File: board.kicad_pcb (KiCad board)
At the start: 4 copper layers, 100 x 100 mm, 90 parts, among them J1 IN1, J2 IN2, J3 OUT1, J4 OUT2, U1 MFRC52202HN1,151, U2 SN74HC595N, U3 MFRC52202HN1,151, U4 MFRC52202HN1,151, U5 MFRC52202HN1,151, Y1 27.12 MHz Crystal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

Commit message: Previous stuff and im now at a point where a single reader circuit should be ready for replecation
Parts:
- removed C14, C16, C30, C44: 100nF, Capacitor_SMD:C_0603_1608Metric
- added C58: 100nF, Capacitor_SMD:C_0603_1608Metric, F.Cu at (104.4, 85.2)
- added C59: 100nF, Capacitor_SMD:C_0603_1608Metric, F.Cu at (214.0, 132.2)
- added C60: 100nF, Capacitor_SMD:C_0603_1608Metric, F.Cu at (184.1, 53.0)
- added C61: 100nF, Capacitor_SMD:C_0603_1608Metric, F.Cu at (190.8, 106.5)
- added C62: 100nF, Capacitor_SMD:C_0603_1608Metric, F.Cu at (100.0, 85.4)
- added C63: 100nF, Capacitor_SMD:C_0603_1608Metric, F.Cu at (214.0, 129.0)
- added C64: 100nF, Capacitor_SMD:C_0603_1608Metric, F.Cu at (187.3, 53.0)
- added C65: 100nF, Capacitor_SMD:C_0603_1608Metric, F.Cu at (190.8, 109.8)
- added C66: 1uF, Capacitor_SMD:C_0603_1608Metric, F.Cu at (104.2, 76.8)
- added C67: 1uF, Capacitor_SMD:C_0603_1608Metric, F.Cu at (223.0, 133.0)
- added C68: 1uF, Capacitor_SMD:C_0603_1608Metric, F.Cu at (183.3, 62.0)
- added C69: 1uF, Capacitor_SMD:C_0603_1608Metric, F.Cu at (181.8, 105.8)
- added R13: 10k, Resistor_SMD:R_0603_1608Metric, F.Cu at (97.7, 87.0)
- added R14: 10k, Resistor_SMD:R_0603_1608Metric, F.Cu at (213.2, 125.0)
- added R15: 10k, Resistor_SMD:R_0603_1608Metric, F.Cu at (191.3, 52.3)
- added R16: 10k, Resistor_SMD:R_0603_1608Metric, F.Cu at (191.5, 113.8)
- J1: footprint Connector_PinSocket_2.54mm:PinSocket_1x09_P2.54mm_Horizontal -> Connector_PinSocket_2.54mm:PinSocket_1x10_P2.54mm_Horizontal
- J2: value IN2 -> OUT1; footprint Connector_PinSocket_2.54mm:PinSocket_1x09_P2.54mm_Horizontal -> Connector_PinSocket_2.54mm:PinSocket_1x10_P2.54mm_Horizontal
- J3: value OUT1 -> IN2; footprint Connector_PinHeader_2.54mm:PinHeader_1x09_P2.54mm_Horizontal -> Connector_PinSocket_2.54mm:PinSocket_1x10_P2.54mm_Horizontal
- J4: footprint Connector_PinHeader_2.54mm:PinHeader_1x09_P2.54mm_Horizontal -> Connector_PinSocket_2.54mm:PinSocket_1x10_P2.54mm_Horizontal
- moved U3 105.5 mm to (218.0, 130.0)
- moved U5 104.2 mm to (186.8, 108.8)
- moved U4 104.2 mm to (186.3, 57.0)
- moved C52 84.3 mm to (183.0, 116.0), turned to 180 degrees
- moved C46 81.6 mm to (190.0, 113.8), turned to -90 degrees
- moved C47 81.0 mm to (186.5, 116.5)
- moved L7 80.5 mm to (182.0, 107.5), turned to 180 degrees
- moved C50 80.4 mm to (177.0, 107.5), turned to 180 degrees
- moved C45 80.3 mm to (180.8, 111.8), turned to -90 degrees
- moved C43 79.8 mm to (188.5, 104.8), turned to 180 degrees
- moved L8 79.7 mm to (182.0, 109.2), turned to 180 degrees
- moved C51 79.7 mm to (177.0, 109.2), turned to 180 degrees
- moved Y4 78.6 mm to (187.0, 113.8)
- moved R11 77.2 mm to (182.2, 111.8), turned to -90 degrees
- moved R12 76.6 mm to (183.8, 113.5), turned to -90 degrees
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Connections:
- C11 pad 1: Net-(C11-Pad1) -> Net-(C10-Pad1)
- C12 pad 2: Net-(C11-Pad1) -> Net-(C10-Pad1)
- C23 pad 2: Net-(C23-Pad2) -> Net-(C22-Pad2)
- C26 pad 1: Net-(C23-Pad2) -> Net-(C22-Pad2)
- C28 pad 2: Net-(C23-Pad2) -> Net-(C22-Pad2)
- C37 pad 2: Net-(C37-Pad2) -> Net-(C36-Pad2)
- C40 pad 1: Net-(C37-Pad2) -> Net-(C36-Pad2)
- C42 pad 2: Net-(C37-Pad2) -> Net-(C36-Pad2)
- C51 pad 2: Net-(C51-Pad2) -> Net-(C50-Pad2)
- C54 pad 1: Net-(C51-Pad2) -> Net-(C50-Pad2)
- C56 pad 2: Net-(C51-Pad2) -> Net-(C50-Pad2)
- C8 pad 2: Net-(C11-Pad1) -> Net-(C10-Pad1)
- J1 pad 7: /Sub Board/SRCLK -> /Sub Board/OE
- J1 pad 8: /Sub Board/RCLK -> /Sub Board/SRCLK
- J1 pad 9: /Sub Board/SER -> /Sub Board/RCLK
- J2 pad 7: /Sub Board/SRCLK -> /Sub Board/OE
- J2 pad 8: /Sub Board/RCLK -> /Sub Board/SRCLK
- J2 pad 9: /Sub Board/SER -> /Sub Board/RCLK
- J3 pad 7: /Sub Board/SRCLK -> /Sub Board/OE
- J3 pad 8: /Sub Board/RCLK -> /Sub Board/SRCLK
- J3 pad 9: /Sub Board/SER_OUT -> /Sub Board/RCLK
- J4 pad 7: /Sub Board/SRCLK -> /Sub Board/OE
- J4 pad 8: /Sub Board/RCLK -> /Sub Board/SRCLK
- J4 pad 9: /Sub Board/SER_OUT -> /Sub Board/RCLK
- U2 pad 13: GND -> /Sub Board/OE
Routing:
- net Net-(C10-Pad1): track 17.1 -> 482.1 mm, vias 2 -> 4
- net GND: track 42.0 -> 153.2 mm, vias 26 -> 101
- net +3V3: track 8.26 -> 47.4 mm, vias 5 -> 22
- net Net-(C50-Pad2): track 0.00 -> 20.5 mm, vias 0 -> 2
- net Net-(C22-Pad2): track 0.00 -> 20.5 mm, vias 0 -> 2
- net Net-(C36-Pad2): track 0.00 -> 20.5 mm, vias 0 -> 2
- net Net-(U3-OSCIN): track 0.00 -> 5.78 mm
- net Net-(U5-OSCIN): track 0.00 -> 5.78 mm
- net Net-(U4-OSCIN): track 0.00 -> 5.78 mm
- net /Sub Board/RC522-1/MFSDA-CS: track 0.00 -> 4.95 mm, vias 0 -> 2
- net /Sub Board/RST: track 1.68 -> 6.37 mm
- net Net-(U4-OSCOUT): track 0.00 -> 3.83 mm
- net Net-(U3-OSCOUT): track 0.00 -> 3.83 mm
- net Net-(U5-OSCOUT): track 0.00 -> 3.83 mm
- net /Sub Board/RC522-3/VMID: track 0.00 -> 3.70 mm
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
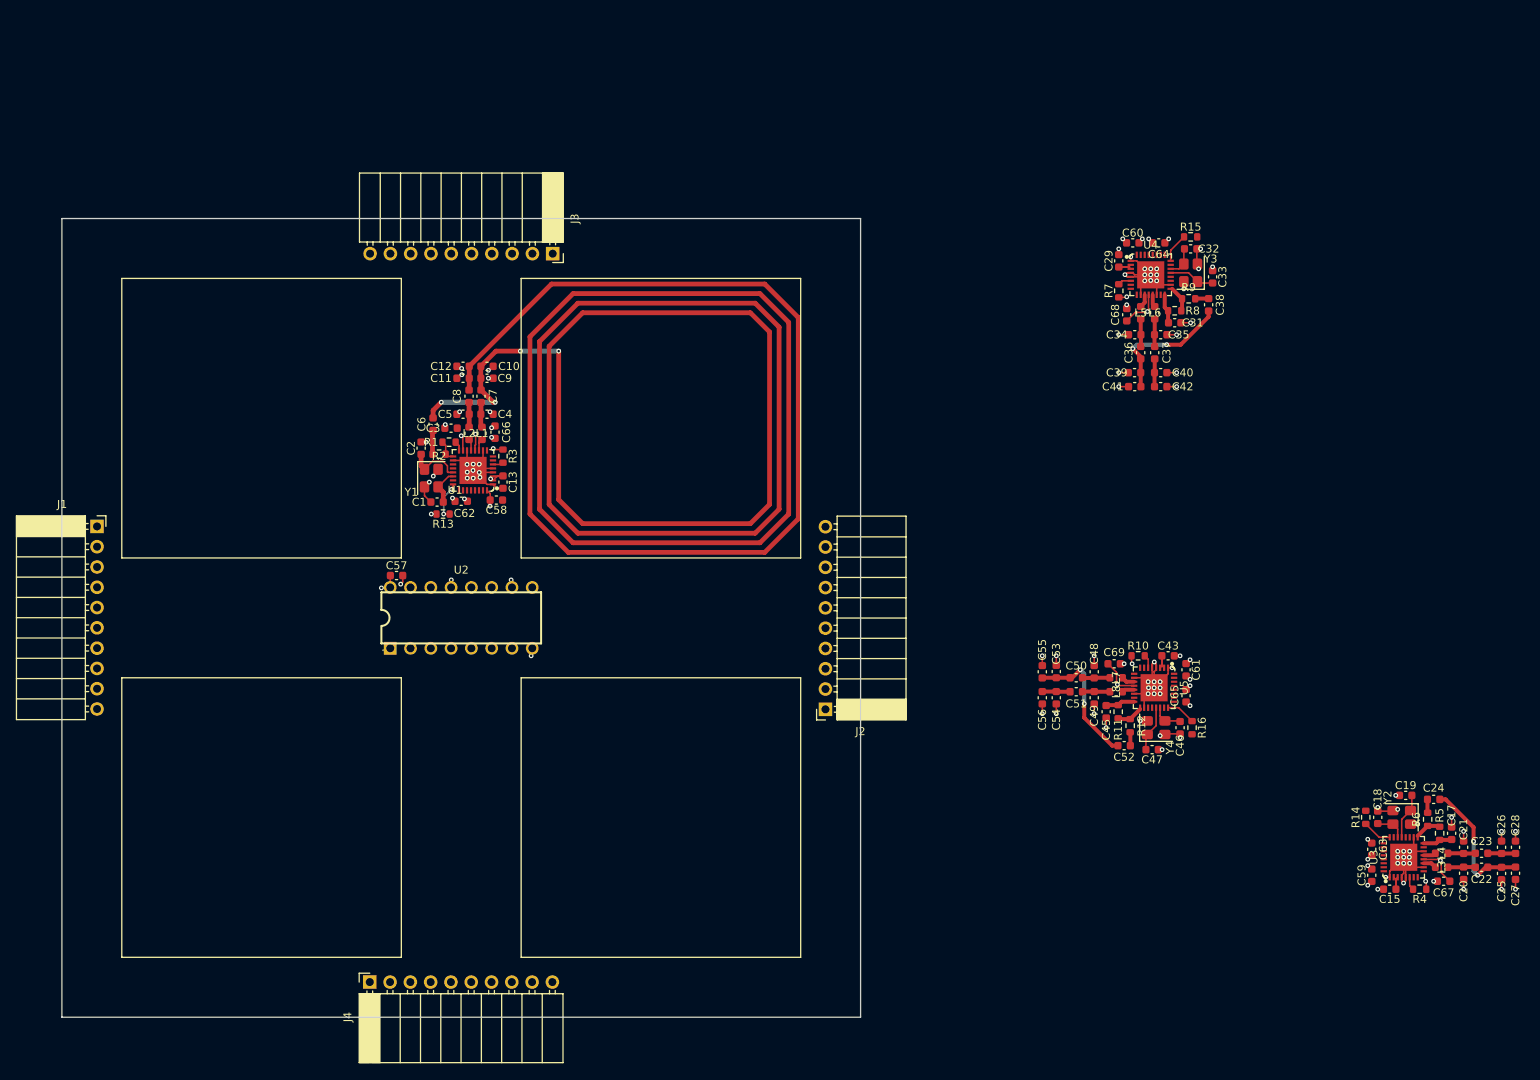
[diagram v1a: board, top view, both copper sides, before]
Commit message: Added non replication-relevant traces and keepout zones
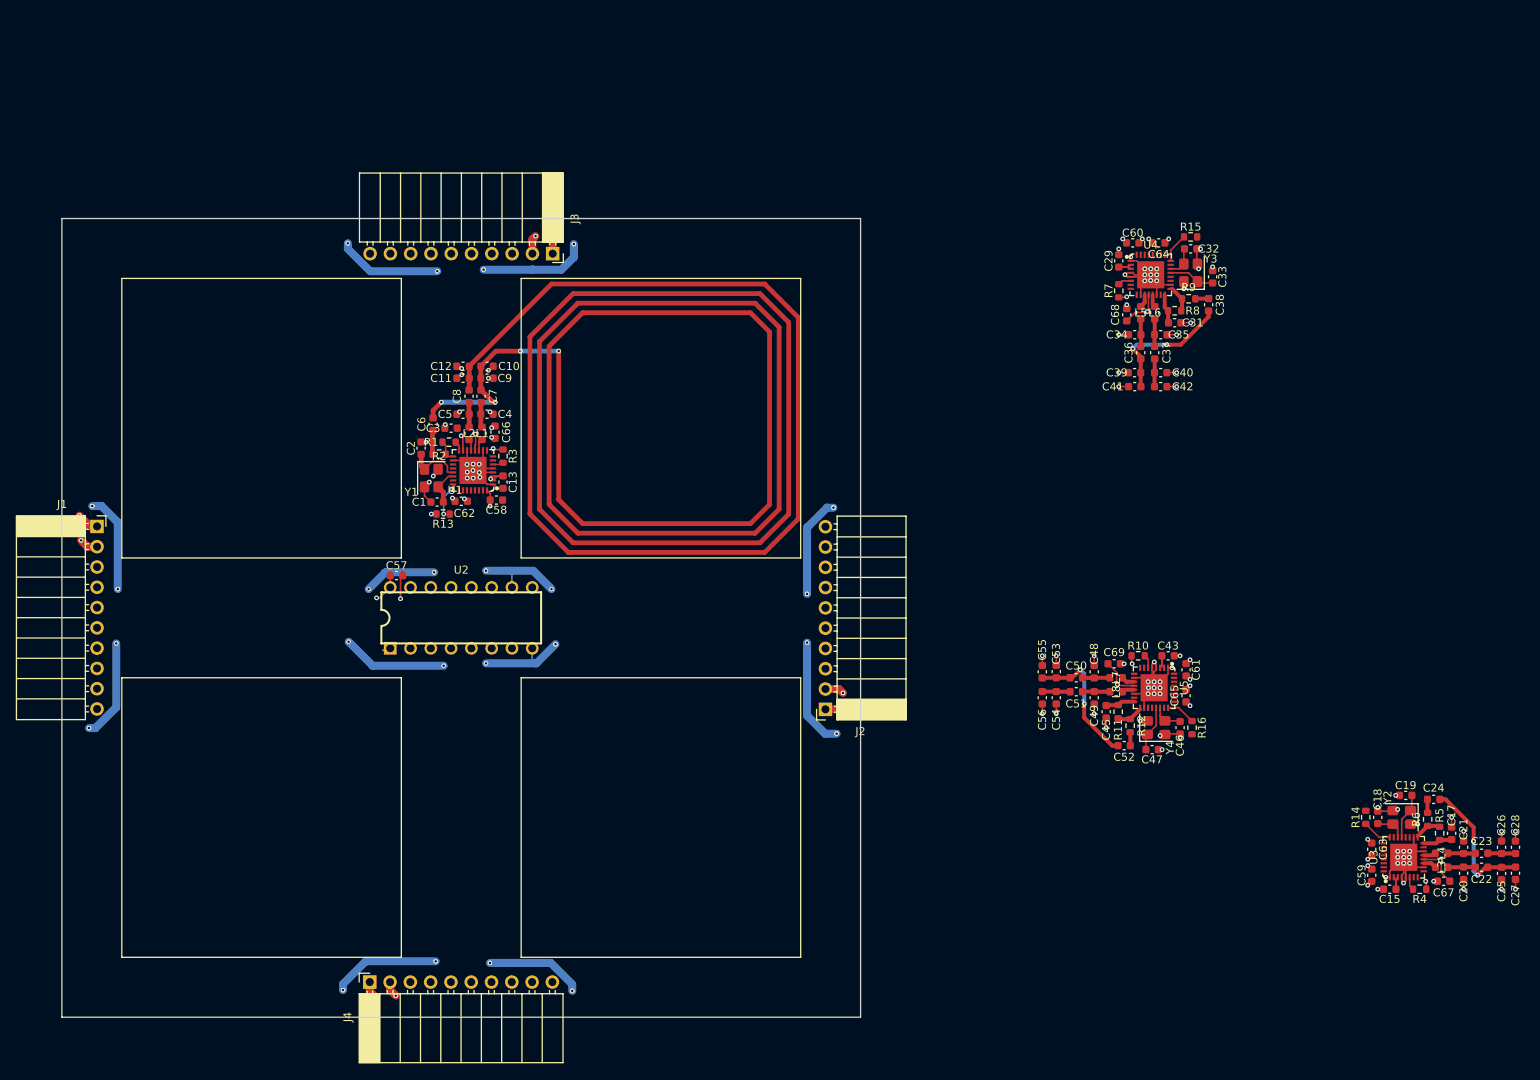
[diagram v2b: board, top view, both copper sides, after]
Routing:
- net +3V3: track 47.4 -> 132.8 mm, vias 22 -> 37
- net GND: track 153.2 -> 237.3 mm, vias 101 -> 116
- net /Sub Board/OE: track 0.95 -> 0.00 mm, vias 1 -> 0

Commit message: Replacted layout and places replicas
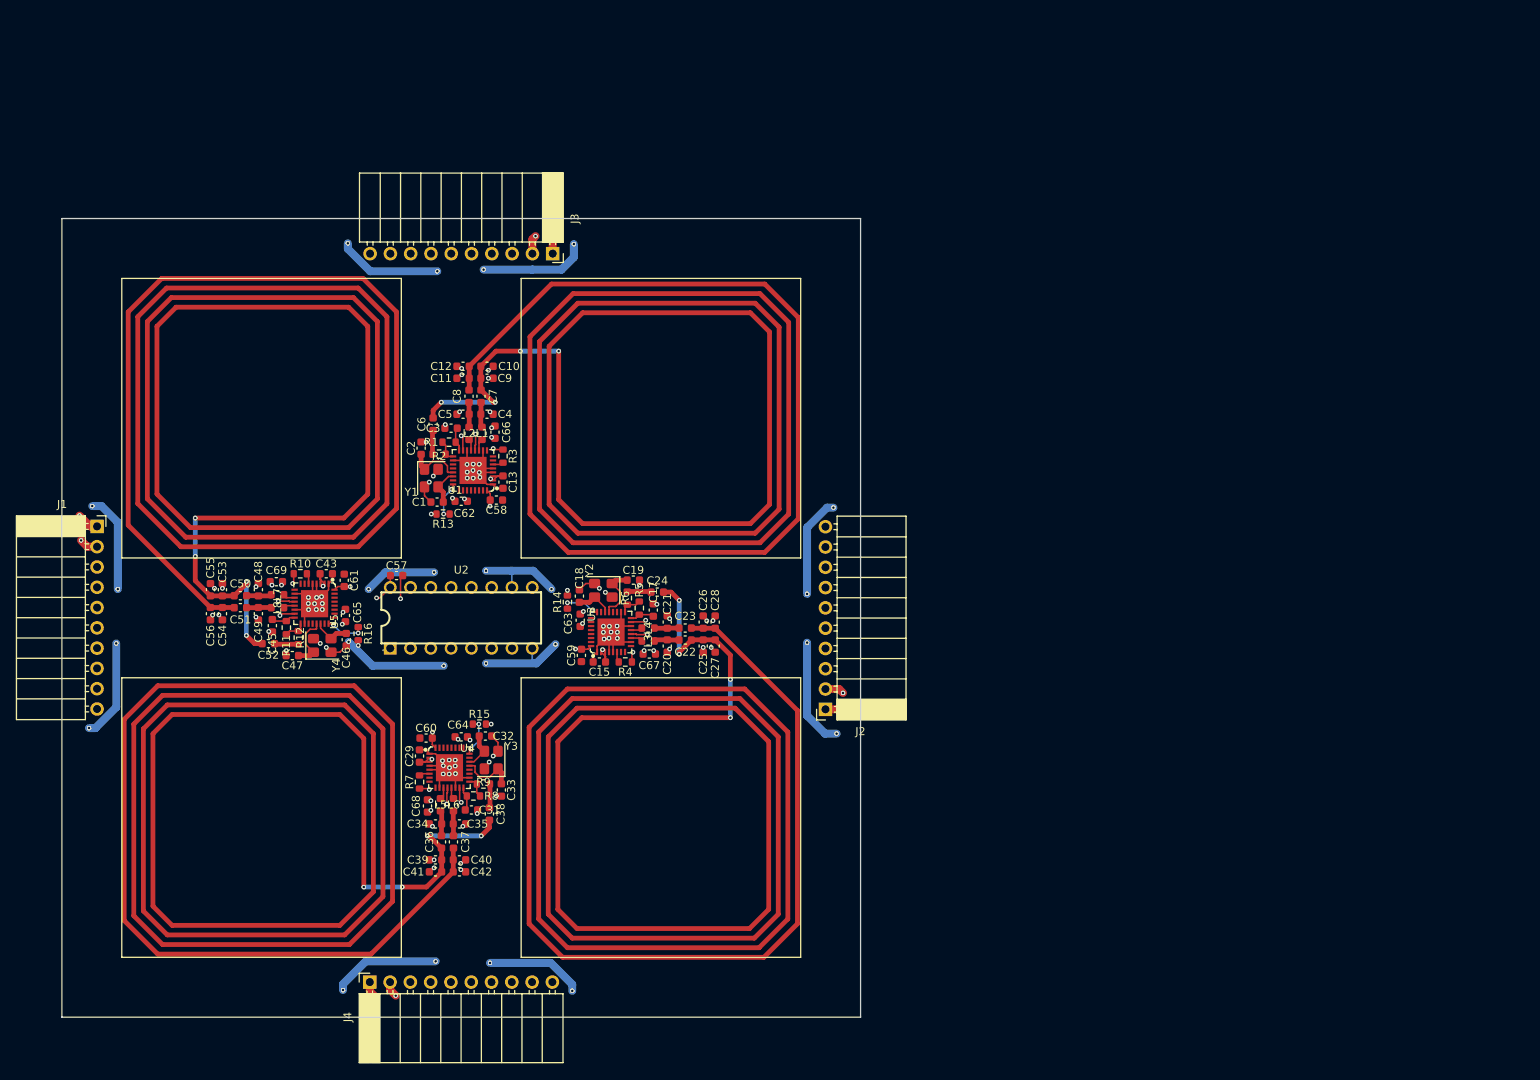
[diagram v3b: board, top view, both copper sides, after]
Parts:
- moved C38 110.3 mm to (103.5, 124.5)
- moved C33 109.8 mm to (105.0, 121.5), turned to -90 degrees
- moved C47 108.3 mm to (78.8, 104.7), turned to 180 degrees
- moved C60 108.0 mm to (95.6, 115.0)
- moved R15 107.9 mm to (102.3, 113.3)
- moved C52 107.9 mm to (75.8, 103.2)
- moved C32 107.3 mm to (103.0, 114.8)
- moved U4 107.3 mm to (98.5, 118.8)
- moved C29 107.3 mm to (94.8, 117.3)
- moved L6 107.3 mm to (99.0, 123.4)
- moved R9 107.2 mm to (102.8, 120.8)
- moved L5 107.2 mm to (97.4, 123.4)
- moved C31 107.1 mm to (101.3, 124.0)
- moved C35 107.1 mm to (99.8, 125.8)
- moved C37 107.1 mm to (99.0, 128.1)
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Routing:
- net Net-(C36-Pad2): track 20.5 -> 482.1 mm, vias 2 -> 4
- net Net-(C22-Pad2): track 20.5 -> 482.1 mm, vias 2 -> 4
- net Net-(C50-Pad2): track 20.5 -> 482.1 mm, vias 2 -> 4
- net GND: track 237.3 -> 217.3 mm, vias 116 -> 101
- net +3V3: track 132.8 -> 137.0 mm, vias 37 -> 49
- net /Sub Board/RC522-1/VMID: track 1.21 -> 3.05 mm
- net Net-(C38-Pad1): track 1.69 -> 3.01 mm
- net Net-(C52-Pad1): track 1.69 -> 3.01 mm
- net Net-(C24-Pad1): track 1.69 -> 3.01 mm
- net Net-(U3-OSCIN): track 5.78 -> 7.06 mm
- net Net-(U5-OSCIN): track 5.78 -> 7.06 mm
- net Net-(U4-OSCIN): track 5.78 -> 7.06 mm
- net /Sub Board/RC522-4/MFSDA-CS: track 3.69 -> 4.95 mm, vias 0 -> 2
- net /Sub Board/RC522-2/MFSDA-CS: track 3.69 -> 4.95 mm, vias 0 -> 2
- net /Sub Board/RC522-3/MFSDA-CS: track 3.69 -> 4.95 mm, vias 0 -> 2
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
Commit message: added all routing (very, very ugly but theoretically done)
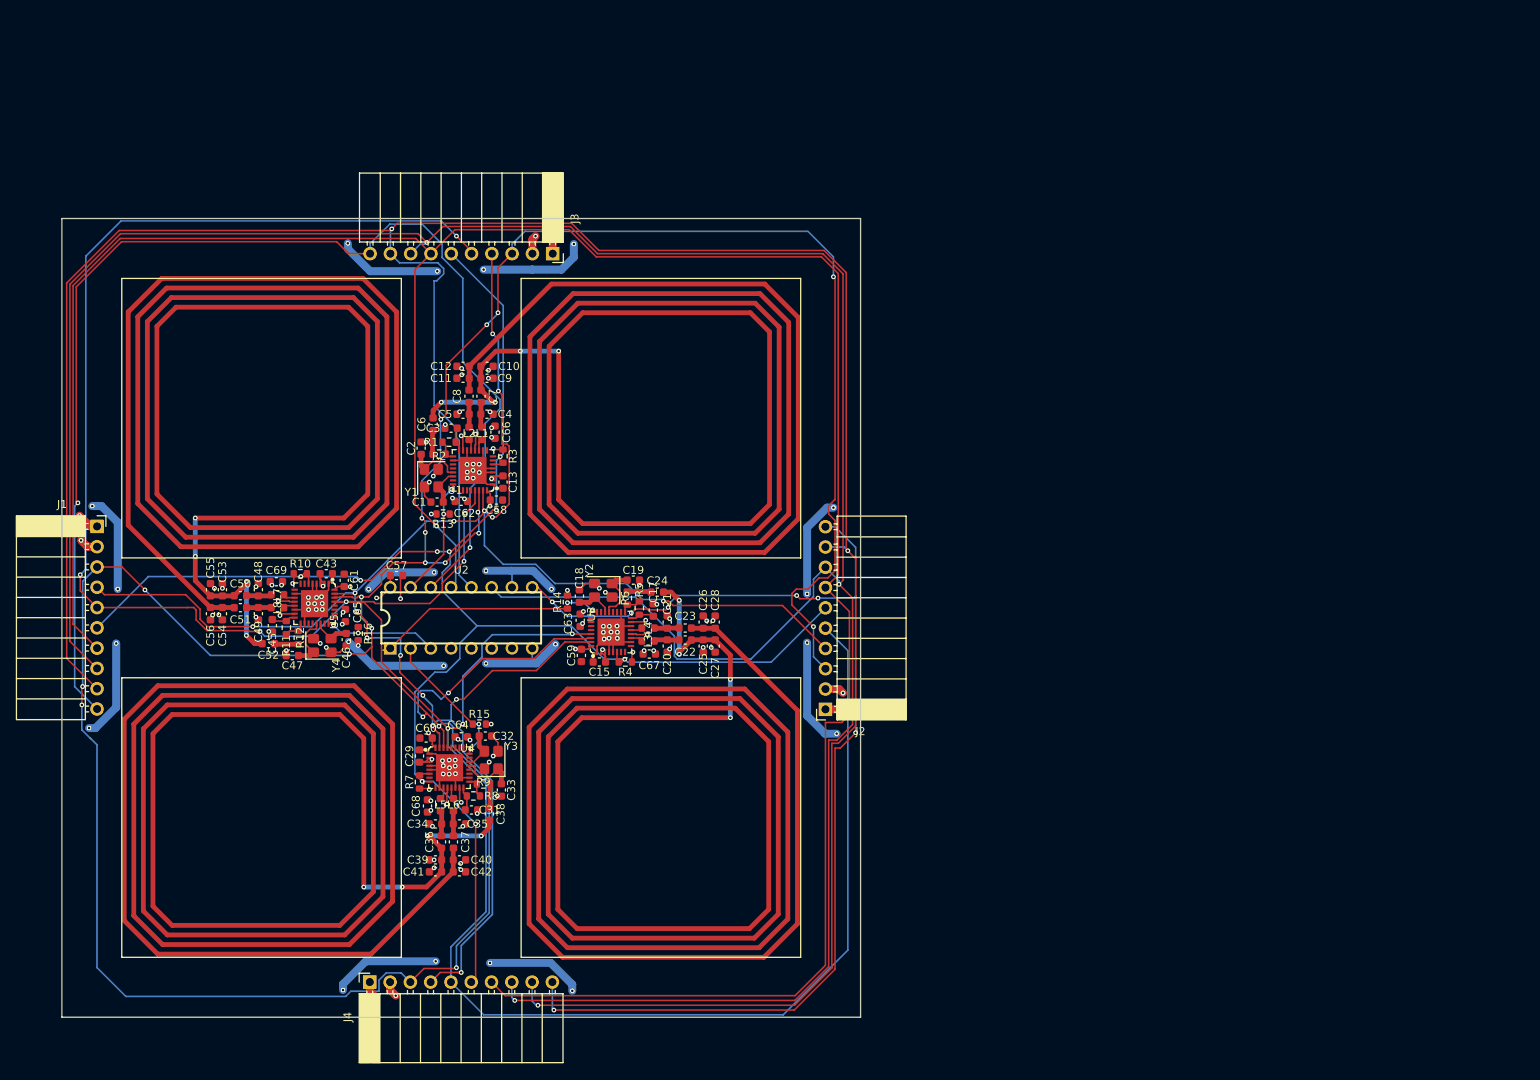
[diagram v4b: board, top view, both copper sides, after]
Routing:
- net /Sub Board/MOSI: track 0.00 -> 401.9 mm, vias 0 -> 21
- net /Sub Board/SCK: track 0.00 -> 346.2 mm, vias 0 -> 9
- net /Sub Board/SRCLK: track 0.00 -> 344.1 mm, vias 0 -> 3
- net /Sub Board/RCLK: track 0.00 -> 343.1 mm, vias 0 -> 3
- net /Sub Board/OE: track 0.00 -> 329.2 mm, vias 0 -> 1
- net /Sub Board/MISO: track 0.00 -> 243.1 mm, vias 0 -> 15
- net /Sub Board/RST: track 5.35 -> 213.3 mm, vias 0 -> 9
- net /Sub Board/SER: track 0.00 -> 155.9 mm, vias 0 -> 2
- net /Sub Board/SER_OUT: track 0.00 -> 143.7 mm, vias 0 -> 7
- net /Sub Board/RC522-2/MFSDA-CS: track 4.95 -> 29.2 mm
- net /Sub Board/RC522-3/MFSDA-CS: track 4.95 -> 17.7 mm
- net /Sub Board/RC522-1/MFSDA-CS: track 4.95 -> 15.9 mm
- net /Sub Board/RC522-4/MFSDA-CS: track 4.95 -> 14.8 mm
- net GND: track 217.3 -> 217.2 mm, vias 101 -> 100
